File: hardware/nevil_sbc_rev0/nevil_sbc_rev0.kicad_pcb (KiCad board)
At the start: 2 copper layers, 72 parts, among them J102 Clock Selector, J301 Enable Pico 3.3V, J302 Expansion Port, J303 VIA0PB, J304 VGA Connector, J305 VIA1PA, J306 VIA1PB, SW101 RESET, U101 74AC00, U102 NE555D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

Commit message: Working on pcb
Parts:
- added J101: Power, Connector_BarrelJack:C9743-CCRNB001R, F.Cu at (-116.8, 63.5)
- added J307: Keyboard, Rhais Connectors:TM 0508 A_6, F.Cu at (234.9, 132.1)
- U203, U205: moved to F.Cu
- moved J304 589.3 mm to (226.6, 91.0), turned to 90 degrees
- moved R304 579.6 mm to (219.7, 110.5), turned to -90 degrees
- moved R316 575.4 mm to (212.1, 81.3), turned to -90 degrees
- moved R303 566.6 mm to (219.7, 120.7), turned to 180 degrees
- moved R313 564.6 mm to (229.9, 120.7), turned to 90 degrees
- moved R309 564.3 mm to (215.9, 95.3), turned to -90 degrees
- moved R315 561.0 mm to (226.1, 120.7), turned to 90 degrees
- moved R312 559.0 mm to (219.7, 81.3), turned to -90 degrees
- moved R311 555.8 mm to (219.7, 91.4), turned to 180 degrees
- moved R308 554.7 mm to (219.7, 95.3), turned to -90 degrees
- moved R307 554.7 mm to (219.7, 105.4), turned to 180 degrees
- moved R314 551.6 mm to (215.9, 81.3), turned to -90 degrees
- moved R305 551.1 mm to (215.9, 110.5), turned to -90 degrees
- moved R310 547.3 mm to (212.1, 95.3), turned to -90 degrees
- moved R302 547.0 mm to (212.1, 110.5), turned to -90 degrees
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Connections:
- J102 pad 1: CLK -> CLKOUT
- J102 pad 2: CLKOUT -> CLK
- R302 pad 2: /IO/pio_rgb_b2 -> /IO/pio_rgb_r2
- R303 pad 2: /IO/pio_rgb_b0 -> /IO/pio_rgb_r0
- R305 pad 2: /IO/pio_rgb_b1 -> /IO/pio_rgb_r1
- R311 pad 2: /IO/pio_rgb_r0 -> /IO/pio_rgb_b0
- R314 pad 2: /IO/pio_rgb_r1 -> /IO/pio_rgb_b1
- R316 pad 2: /IO/pio_rgb_r2 -> /IO/pio_rgb_b2
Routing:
- net d0: track 0.00 -> 50.7 mm

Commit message: Update pcb
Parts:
- moved U207 28.7 mm to (112.3, 157.7)
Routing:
- net d7: track 0.00 -> 159.7 mm, vias 0 -> 1
- net d6: track 0.00 -> 156.4 mm, vias 0 -> 1
- net d5: track 0.00 -> 153.9 mm, vias 0 -> 1
- net d4: track 0.00 -> 149.9 mm, vias 0 -> 1
- net d3: track 0.00 -> 146.0 mm, vias 0 -> 2
- net d2: track 0.00 -> 143.3 mm, vias 0 -> 1
- net d1: track 0.00 -> 140.0 mm, vias 0 -> 1
- net d0: track 50.7 -> 137.9 mm, vias 0 -> 1

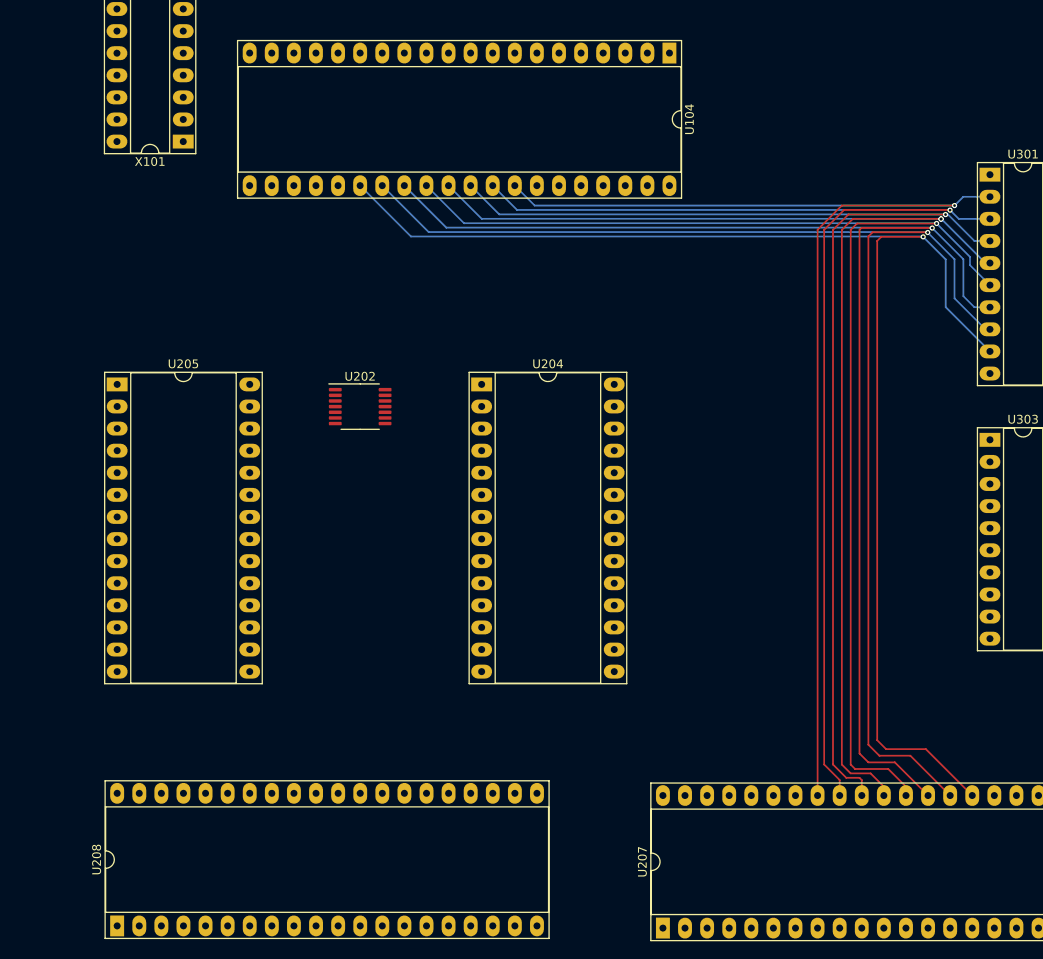
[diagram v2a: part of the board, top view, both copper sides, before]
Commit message: Working on PCB address bus
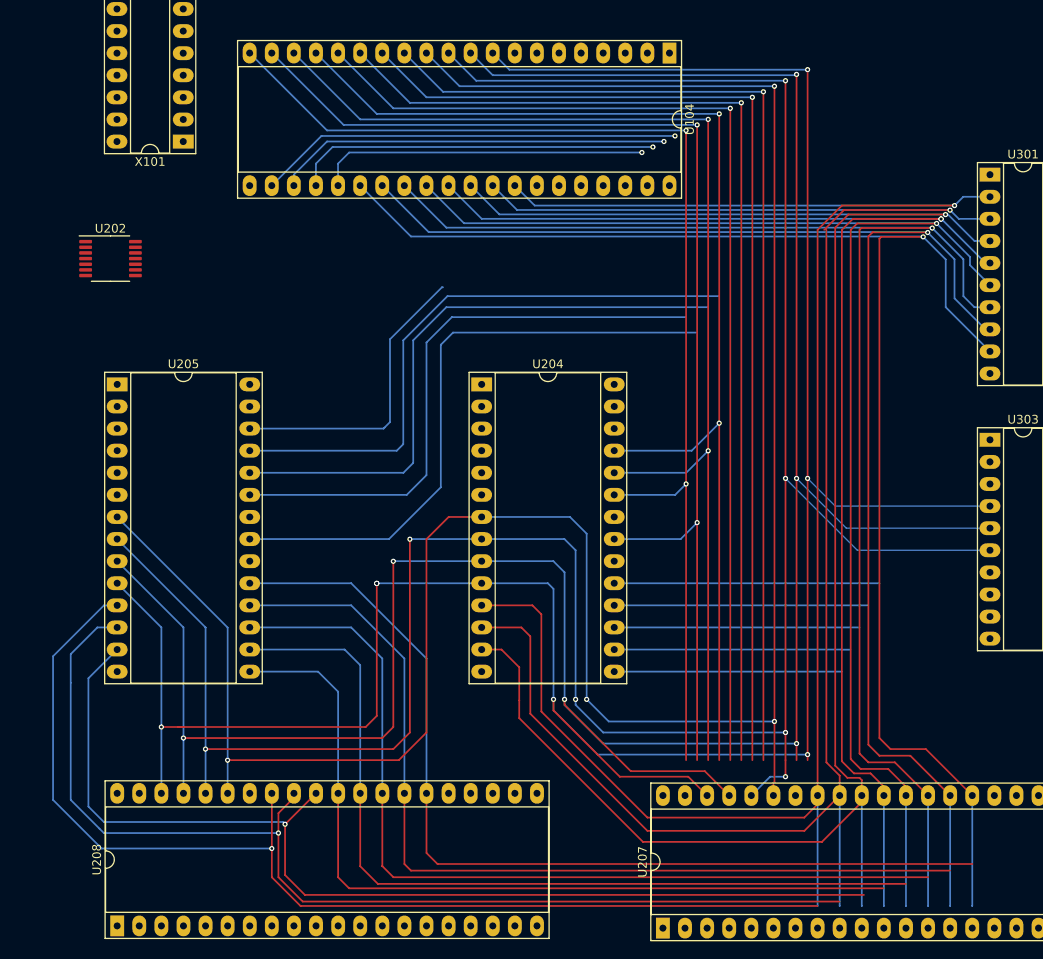
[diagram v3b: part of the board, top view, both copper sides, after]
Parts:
- moved U202 33.4 mm to (48.8, 80.8)
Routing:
- net a1: track 0.00 -> 303.4 mm, vias 0 -> 6
- net a2: track 0.00 -> 295.5 mm, vias 0 -> 7
- net a0: track 0.00 -> 294.9 mm, vias 0 -> 7
- net a3: track 0.00 -> 268.6 mm, vias 0 -> 4
- net a10: track 0.00 -> 206.5 mm, vias 0 -> 2
- net a8: track 0.00 -> 205.3 mm, vias 0 -> 2
- net a9: track 0.00 -> 205.1 mm, vias 0 -> 2
- net a11: track 0.00 -> 202.6 mm, vias 0 -> 2
- net d0: track 137.9 -> 335.1 mm, vias 1 -> 2
- net d1: track 140.0 -> 335.2 mm, vias 1 -> 2
- net d2: track 143.3 -> 335.9 mm, vias 1 -> 2
- net d7: track 159.7 -> 311.9 mm
- net d6: track 156.4 -> 305.3 mm
- net d5: track 153.9 -> 298.6 mm
- net d4: track 149.9 -> 289.6 mm
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
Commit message: working on vga code
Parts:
- added H101: M3 Mounting Hole, MountingHole:MountingHole_3.2mm_M3_Pad, F.Cu at (178.2, 118.5)
- added H102: M3 Mounting Hole, MountingHole:MountingHole_3.2mm_M3_Pad, F.Cu at (51.2, 24.3)
- added H103: Expansion Support, MountingHole:MountingHole_3.2mm_M3_Pad, F.Cu at (237.3, 165.0)
- added H104: M3 Mounting Hole, MountingHole:MountingHole_3.2mm_M3_Pad, F.Cu at (51.2, 140.9)
- added H105: M3 Mounting Hole, MountingHole:MountingHole_3.2mm_M3_Pad, F.Cu at (237.3, 24.3)
- U202: footprint Package_SO:TSSOP-14_4.4x5mm_P0.65mm -> Package_SO:TSSOP-16_4.4x5mm_P0.65mm
- moved R102 717.3 mm to (194.3, 46.8), turned to 90 degrees
- moved C207 717.1 mm to (217.5, 165.0)
- moved R109 714.2 mm to (216.1, 53.4), turned to 180 degrees
- moved D101 706.3 mm to (216.2, 49.8), turned to 90 degrees
- moved R101 699.7 mm to (194.3, 29.5), turned to -90 degrees
- moved C102 696.4 mm to (210.7, 37.0), turned to 180 degrees
- moved C104 689.3 mm to (186.3, 50.0), turned to 180 degrees
- moved C209 687.3 mm to (207.1, 164.9)
- moved U102 660.5 mm to (186.8, 33.6), turned to 90 degrees
- moved C101 658.6 mm to (210.7, 47.2), turned to 180 degrees
- moved C105 646.0 mm to (186.3, 25.5), turned to 90 degrees
- moved R201 645.2 mm to (145.5, 160.5), turned to 180 degrees
- moved SW101 639.4 mm to (181.7, 46.7), turned to 90 degrees
- moved R103 638.3 mm to (138.1, 44.5), turned to 90 degrees
- moved C103 632.2 mm to (180.7, 30.1), turned to -90 degrees
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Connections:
- J302 pad 30: ~{EXT_IRQ} -> ~{EXT_IO_IRQ}
- J302 pad 31: a15 -> ~{RAM}
- J304 pad 0: unconnected-(J304-Pad0) -> GND
- R301 pad 1: ~{EXT_IRQ} -> ~{EXT_IO_IRQ}
- U303 pad 13: PIO_CLK -> unconnected-(U303-Pad13)
- U303 pad 7: CLK -> unconnected-(U303-Pad7)
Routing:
- net +5V: track 0.00 -> 943.2 mm, vias 0 -> 18
- net CLK: track 0.00 -> 456.1 mm, vias 0 -> 5
- net R/~{W}: track 0.00 -> 350.6 mm, vias 0 -> 4
- net ~{RESET}: track 0.00 -> 314.5 mm, vias 0 -> 4
- net IO: track 0.00 -> 312.0 mm, vias 0 -> 6
- net ~{VIA0_IRQ}: track 0.00 -> 270.7 mm, vias 0 -> 4
- net ~{VIA1_IRQ}: track 0.00 -> 247.8 mm, vias 0 -> 3
- net ~{EXT_IO_IRQ}: track 0.00 -> 234.4 mm, vias 0 -> 6
- net ~{RD}: track 0.00 -> 231.8 mm, vias 0 -> 2
- net ~{RAM}: track 38.0 -> 263.6 mm, vias 1 -> 6
- net a14: track 42.1 -> 263.7 mm, vias 1 -> 4
- net ~{VIA0}: track 0.00 -> 211.8 mm, vias 0 -> 3
- net ~{VIA1}: track 0.00 -> 211.2 mm, vias 0 -> 3
- net a12: track 48.7 -> 258.9 mm, vias 1 -> 4
- net ~{EXT_IO1}: track 0.00 -> 202.9 mm, vias 0 -> 4
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- added copper zone on B.Cu, net GND
- added copper zone on F.Cu, net GND
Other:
- board outline added: 201.8 x 160 mm
- board text added: "0x8000...0x800F - VIA0 0x8010...0x801F - VIA1 0x8020...0x802F - PicoVGA 0x8030...0x803F - EXT_IO_0 0x8040...0x804F - EXT_IO_1 0x8050...0x805F - EXT_IO_2"
- board text added: "JLCJLCJLCJLC"
- board text added: "Love you Nienke <3"
- board text added: "NotEvils 6502 SBC"
- board text added: "Version 0 Rev 0"
